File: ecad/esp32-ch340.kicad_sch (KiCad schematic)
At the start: 1 part, among them U2 ESP32-WROOM-32

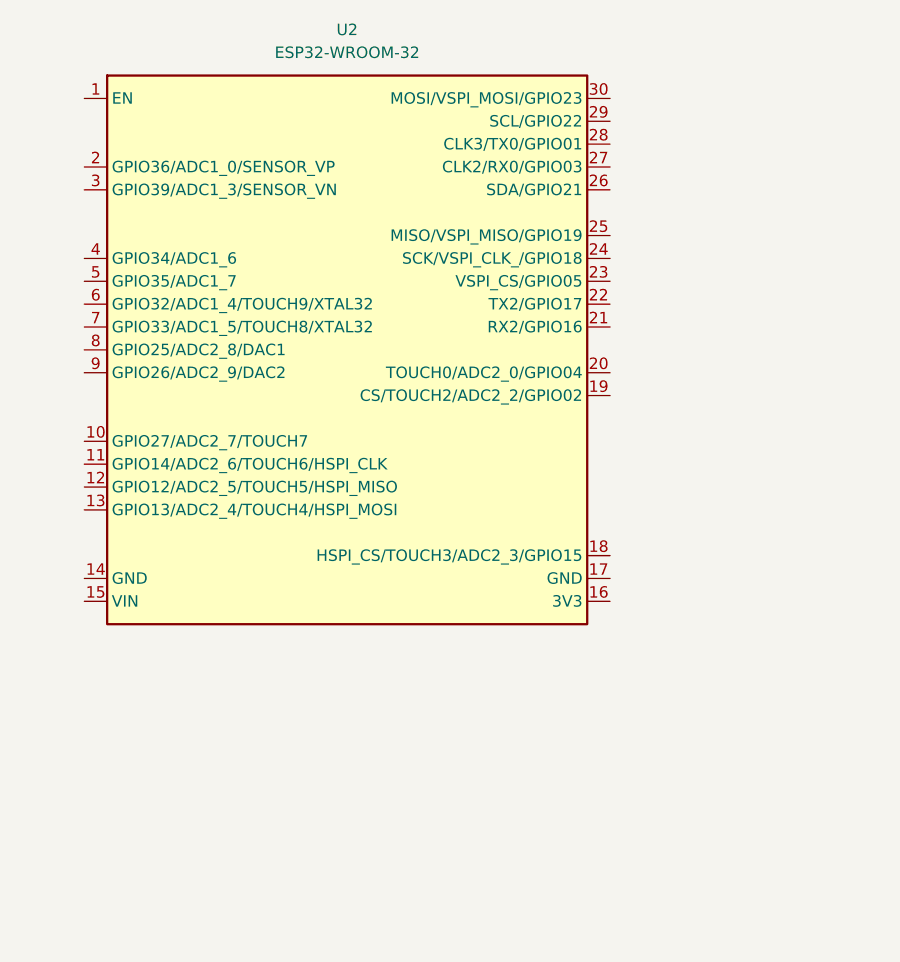
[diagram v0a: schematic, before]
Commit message: fead (ecad): update ESP32-CH340 Schematic
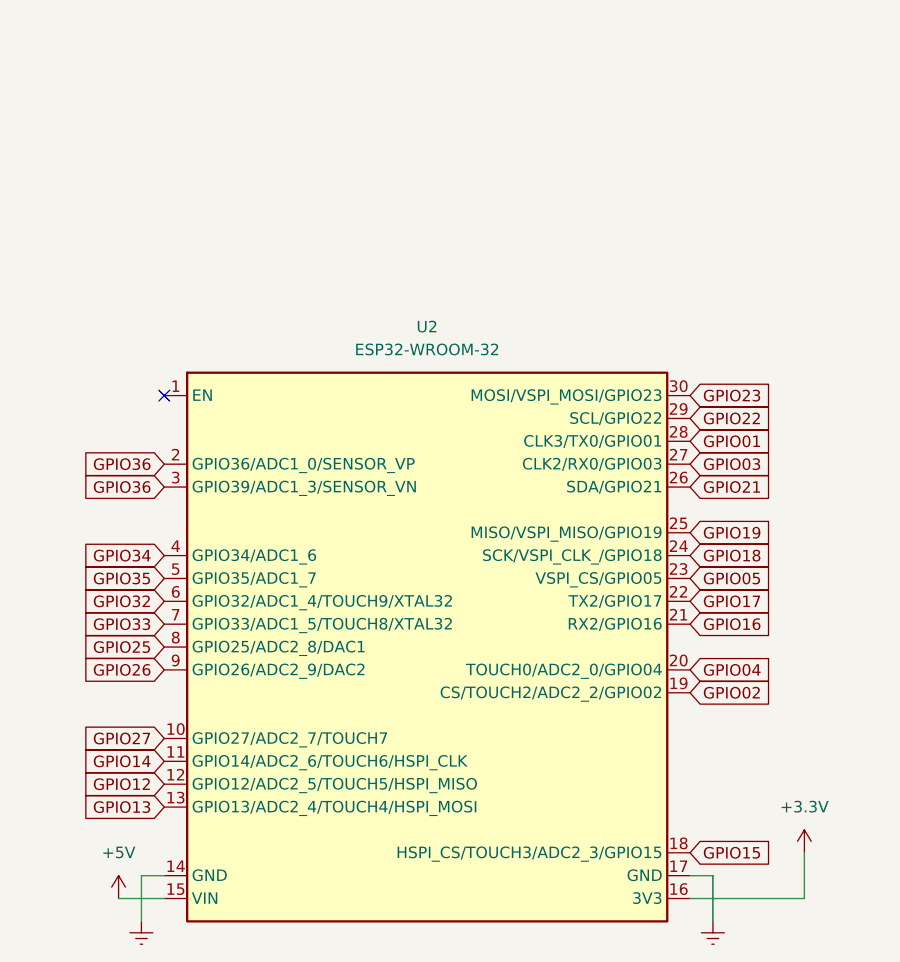
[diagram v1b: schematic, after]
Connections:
- net GPIO27: now reaches U2.10 (GPIO27/ADC2_7/TOUCH7)
- net GPIO14: now reaches U2.11 (GPIO14/ADC2_6/TOUCH6/HSPI_CLK)
- net GPIO12: now reaches U2.12 (GPIO12/ADC2_5/TOUCH5/HSPI_MISO)
- net GPIO13: now reaches U2.13 (GPIO13/ADC2_4/TOUCH4/HSPI_MOSI)
- net Earth: now reaches U2.14 (GND)
- net Earth: now also U2.17 (GND)
- net +5V: now reaches U2.15 (VIN)
- net +3.3V: now reaches U2.16 (3V3)
- net GPIO15: now reaches U2.18 (HSPI_CS/TOUCH3/ADC2_3/GPIO15)
- net GPIO02: now reaches U2.19 (CS/TOUCH2/ADC2_2/GPIO02)
- net GPIO36: now reaches U2.2 (GPIO36/ADC1_0/SENSOR_VP)
- net GPIO36: now also U2.3 (GPIO39/ADC1_3/SENSOR_VN)
- net GPIO04: now reaches U2.20 (TOUCH0/ADC2_0/GPIO04)
- net GPIO16: now reaches U2.21 (RX2/GPIO16)
- net GPIO17: now reaches U2.22 (TX2/GPIO17)
- net GPIO05: now reaches U2.23 (VSPI_CS/GPIO05)
- net GPIO18: now reaches U2.24 (SCK/VSPI_CLK_/GPIO18)
- net GPIO19: now reaches U2.25 (MISO/VSPI_MISO/GPIO19)
- net GPIO21: now reaches U2.26 (SDA/GPIO21)
- net GPIO03: now reaches U2.27 (CLK2/RX0/GPIO03)
- net GPIO01: now reaches U2.28 (CLK3/TX0/GPIO01)
- net GPIO22: now reaches U2.29 (SCL/GPIO22)
- net GPIO23: now reaches U2.30 (MOSI/VSPI_MOSI/GPIO23)
- net GPIO34: now reaches U2.4 (GPIO34/ADC1_6)
- net GPIO35: now reaches U2.5 (GPIO35/ADC1_7)
- net GPIO32: now reaches U2.6 (GPIO32/ADC1_4/TOUCH9/XTAL32)
- net GPIO33: now reaches U2.7 (GPIO33/ADC1_5/TOUCH8/XTAL32)
- net GPIO25: now reaches U2.8 (GPIO25/ADC2_8/DAC1)
- net GPIO26: now reaches U2.9 (GPIO26/ADC2_9/DAC2)
- no-connect marks 0 -> 1
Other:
- title: (none) -> ESP32 AK Shield Schematik drawing CH340
- moved on the sheet: U2

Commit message: feat (ecad): start PCB design
Left header pins and LEDs connected to devkits without ground-voltage
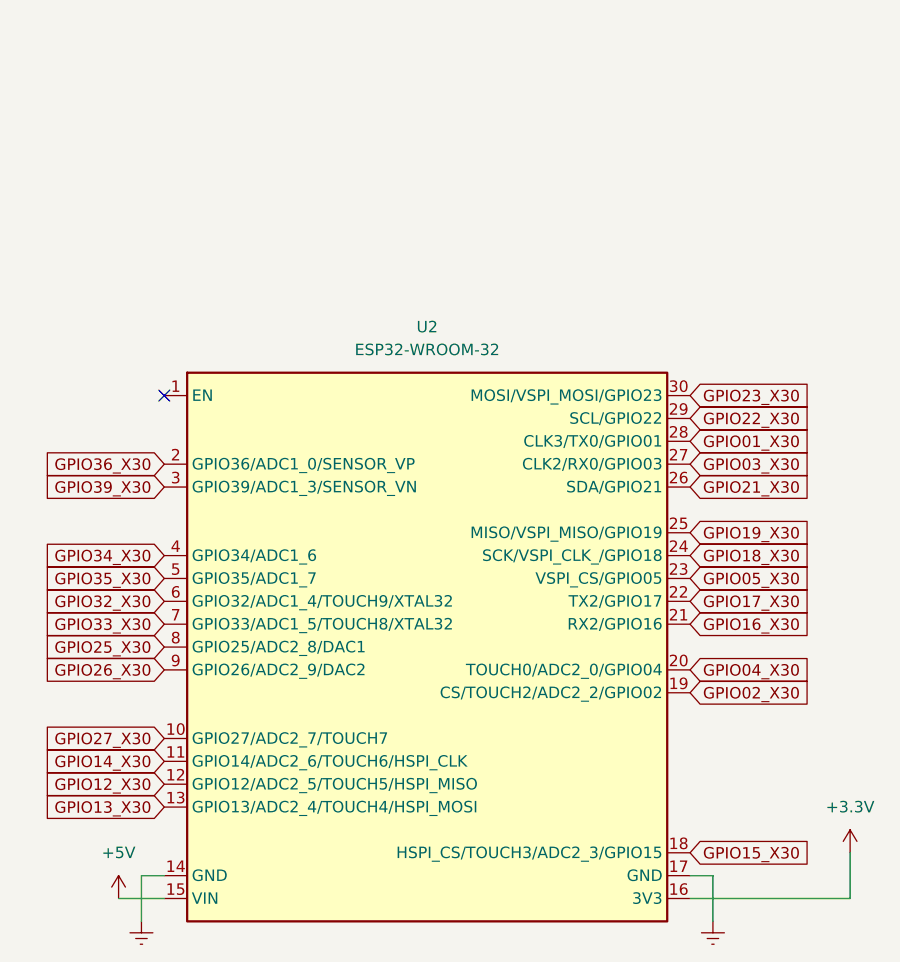
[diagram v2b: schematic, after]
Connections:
- net GPIO01 renamed GPIO01_X30
- net GPIO02 renamed GPIO02_X30
- net GPIO03 renamed GPIO03_X30
- net GPIO04 renamed GPIO04_X30
- net GPIO05 renamed GPIO05_X30
- net GPIO12 renamed GPIO12_X30
- net GPIO13 renamed GPIO13_X30
- net GPIO14 renamed GPIO14_X30
- net GPIO15 renamed GPIO15_X30
- net GPIO16 renamed GPIO16_X30
- net GPIO17 renamed GPIO17_X30
- net GPIO18 renamed GPIO18_X30
- net GPIO19 renamed GPIO19_X30
- net GPIO21 renamed GPIO21_X30
- net GPIO22 renamed GPIO22_X30
- net GPIO23 renamed GPIO23_X30
- net GPIO25 renamed GPIO25_X30
- net GPIO26 renamed GPIO26_X30
- net GPIO27 renamed GPIO27_X30
- net GPIO32 renamed GPIO32_X30
- net GPIO33 renamed GPIO33_X30
- net GPIO34 renamed GPIO34_X30
- net GPIO35 renamed GPIO35_X30
- net GPIO36 renamed GPIO36_X30
- net GPIO36_X30: no longer U2.3 (GPIO39/ADC1_3/SENSOR_VN)
- new net GPIO39_X30: U2.3 (GPIO39/ADC1_3/SENSOR_VN)
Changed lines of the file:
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@@
 	(wire
 		(pts
-			(xy 113.03 111.76) (xy 113.03 106.68)
+			(xy 118.11 111.76) (xy 118.11 106.68)
 		)
 		(stroke
@@
 	(wire
 		(pts
-			(xy 100.33 111.76) (xy 113.03 111.76)
+			(xy 100.33 111.76) (xy 118.11 111.76)
 		)
 		(stroke
@@
 		)
 	)
-	(global_label "GPIO01"
+	(global_label "GPIO01_X30"
 		(shape input)
 		(at 100.33 60.96 0)
@@
 		)
 	)
-	(global_label "GPIO36"
+	(global_label "GPIO39_X30"
 		(shape input)
 		(at 41.91 66.04 180)
@@
 		)
 	)
-	(global_label "GPIO16"
+	(global_label "GPIO16_X30"
 		(shape input)
 		(at 100.33 81.28 0)
@@
 		)
 	)
-	(global_label "GPIO27"
+	(global_label "GPIO27_X30"
 		(shape input)
 		(at 41.91 93.98 180)
@@
 		)
 	)
-	(global_label "GPIO21"
+	(global_label "GPIO21_X30"
 		(shape input)
 		(at 100.33 66.04 0)
@@
 		)
 	)
-	(global_label "GPIO17"
+	(global_label "GPIO17_X30"
 		(shape input)
 		(at 100.33 78.74 0)
@@
 		)
 	)
-	(global_label "GPIO04"
+	(global_label "GPIO04_X30"
 		(shape input)
 		(at 100.33 86.36 0)
@@
 		)
 	)
-	(global_label "GPIO36"
+	(global_label "GPIO36_X30"
 		(shape input)
 		(at 41.91 63.5 180)
@@
 		)
 	)
-	(global_label "GPIO33"
+	(global_label "GPIO33_X30"
 		(shape input)
 		(at 41.91 81.28 180)
@@
 		)
 	)
-	(global_label "GPIO13"
+	(global_label "GPIO13_X30"
 		(shape input)
 		(at 41.91 101.6 180)
@@
 		)
 	)
-	(global_label "GPIO03"
+	(global_label "GPIO03_X30"
 		(shape input)
 		(at 100.33 63.5 0)
@@
 		)
 	)
-	(global_label "GPIO19"
+	(global_label "GPIO19_X30"
 		(shape input)
 		(at 100.33 71.12 0)
@@
 		)
 	)
-	(global_label "GPIO34"
+	(global_label "GPIO34_X30"
 		(shape input)
 		(at 41.91 73.66 180)
@@
 		)
 	)
-	(global_label "GPIO02"
+	(global_label "GPIO02_X30"
 		(shape input)
 		(at 100.33 88.9 0)
@@
 		)
 	)
-	(global_label "GPIO23"
+	(global_label "GPIO23_X30"
 		(shape input)
 		(at 100.33 55.88 0)
@@
 		)
 	)
-	(global_label "GPIO12"
+	(global_label "GPIO12_X30"
 		(shape input)
 		(at 41.91 99.06 180)
@@
 		)
 	)
-	(global_label "GPIO18"
+	(global_label "GPIO18_X30"
 		(shape input)
 		(at 100.33 73.66 0)
@@
 		)
 	)
-	(global_label "GPIO32"
+	(global_label "GPIO32_X30"
 		(shape input)
 		(at 41.91 78.74 180)
@@
 		)
 	)
-	(global_label "GPIO05"
+	(global_label "GPIO05_X30"
 		(shape input)
 		(at 100.33 76.2 0)
@@
 		)
 	)
-	(global_label "GPIO22"
+	(global_label "GPIO22_X30"
 		(shape input)
 		(at 100.33 58.42 0)
@@
 		)
 	)
-	(global_label "GPIO15"
+	(global_label "GPIO15_X30"
 		(shape input)
 		(at 100.33 106.68 0)
@@
 		)
 	)
-	(global_label "GPIO14"
+	(global_label "GPIO14_X30"
 		(shape input)
 		(at 41.91 96.52 180)
@@
 		)
 	)
-	(global_label "GPIO35"
+	(global_label "GPIO35_X30"
 		(shape input)
 		(at 41.91 76.2 180)
@@
 		)
 	)
-	(global_label "GPIO26"
+	(global_label "GPIO26_X30"
 		(shape input)
 		(at 41.91 86.36 180)
@@
 		)
 	)
-	(global_label "GPIO25"
+	(global_label "GPIO25_X30"
 		(shape input)
 		(at 41.91 83.82 180)
@@
 	(symbol
 		(lib_id "power:+3.3V")
-		(at 113.03 106.68 0)
+		(at 118.11 106.68 0)
 		(unit 1)
 		(exclude_from_sim no)
@@
 		(fields_autoplaced yes)
 		(property "Reference" "#PWR09"
-			(at 113.03 110.49 0)
+			(at 118.11 110.49 0)
 			(effects
 				(font
@@
 		)
 		(property "Value" "+3.3V"
-			(at 113.03 101.6 0)
+			(at 118.11 101.6 0)
 			(effects
 				(font
@@
 		)
 		(property "Footprint" ""
-			(at 113.03 106.68 0)
+			(at 118.11 106.68 0)
 			(effects
 				(font
@@
 		)
 		(property "Datasheet" ""
-			(at 113.03 106.68 0)
+			(at 118.11 106.68 0)
 			(effects
 				(font
@@
 		)
 		(property "Description" "Power symbol creates a global label with name \"+3.3V\""
-			(at 113.03 106.68 0)
-			(effects
-				(font
+			(at 118.11 106.68 0)
+			(effects
+				(font
